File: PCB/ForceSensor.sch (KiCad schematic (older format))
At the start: 8 parts

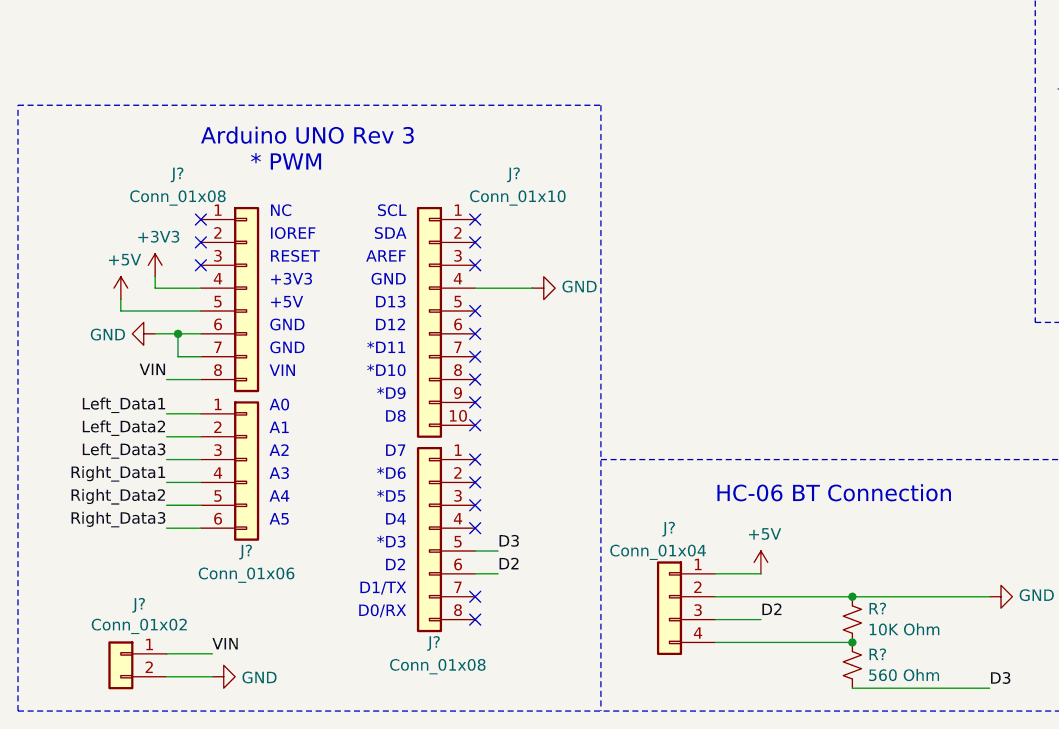
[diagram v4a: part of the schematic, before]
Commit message: Rough layout of pcb
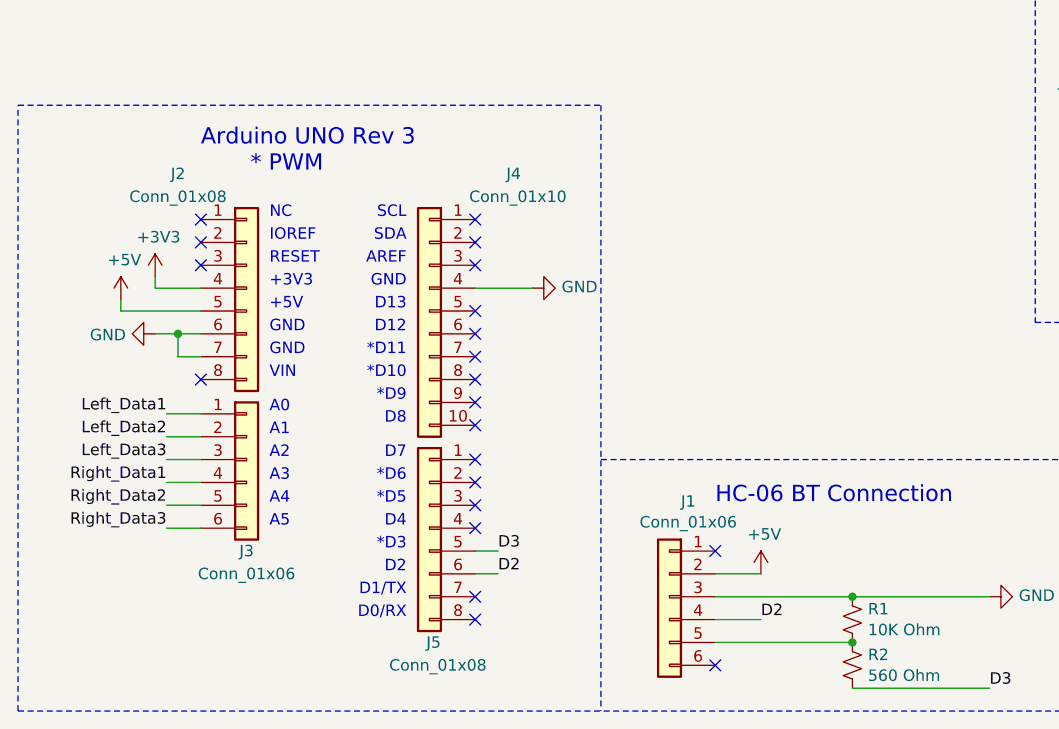
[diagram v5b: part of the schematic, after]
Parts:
- removed J?: Conn_01x04, symbol Connector_Generic:Conn_01x04
- removed J?: Conn_01x02, symbol Connector_Generic:Conn_01x02
- added J1: Conn_01x06, Connector_PinHeader_2.54mm:PinHeader_1x06_P2.54mm_Vertical, symbol Connector_Generic:Conn_01x06
- J2, J5: renamed from J?; footprint (none) -> Connector_PinHeader_2.54mm:PinHeader_1x08_P2.54mm_Vertical
- J3: renamed from J?; footprint (none) -> Connector_PinHeader_2.54mm:PinHeader_1x06_P2.54mm_Vertical
- J4: renamed from J?; footprint (none) -> Connector_PinHeader_2.54mm:PinHeader_1x10_P2.54mm_Vertical
- R1, R2: renamed from R?; footprint (none) -> Resistor_THT:R_Axial_DIN0207_L6.3mm_D2.5mm_P7.62mm_Horizontal
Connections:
- net +5V: now also J1.2 (Pin_2)
- net D2: now also J1.4 (Pin_4)
- net GND: now also J1.3 (Pin_3)
- net at R1.2, R2.1: now also J1.5 (Pin_5)
- net VIN: no longer names the net of J2.8 (Pin_8)
- no-connect marks 18 -> 21
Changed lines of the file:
@@
 $EndDescr
 $Comp
-L Connector_Generic:Conn_01x10 J?
+L Connector_Generic:Conn_01x10 J4
 U 1 1 611AFD66
 P 3850 3100
-F 0 "J?" H 3450 3700 50  0000 L CNN
+F 0 "J4" H 3450 3700 50  0000 L CNN
 F 1 "Conn_01x10" H 3250 3600 50  0000 L CNN
-F 2 "" H 3850 3100 50  0001 C CNN
+F 2 "Connector_PinHeader_2.54mm:PinHeader_1x10_P2.54mm_Vertical" H 3850 3100 50  0001 C CNN
 F 3 "~" H 3850 3100 50  0001 C CNN
 	1    3850 3100
@@
 $EndSheet
 $Comp
-L Connector_Generic:Conn_01x08 J?
+L Connector_Generic:Conn_01x08 J2
 U 1 1 611E4224
 P 3050 3000
-F 0 "J?" H 2750 3500 50  0000 C CNN
+F 0 "J2" H 2750 3500 50  0000 C CNN
 F 1 "Conn_01x08" H 2750 3400 50  0000 C CNN
-F 2 "" H 3050 3000 50  0001 C CNN
+F 2 "Connector_PinHeader_2.54mm:PinHeader_1x08_P2.54mm_Vertical" H 3050 3000 50  0001 C CNN
 F 3 "~" H 3050 3000 50  0001 C CNN
 	1    3050 3000
@@
 $EndComp
 $Comp
-L Connector_Generic:Conn_01x06 J?
+L Connector_Generic:Conn_01x06 J3
 U 1 1 611E4D84
 P 3050 3750
-F 0 "J?" H 3050 3350 50  0000 C CNN
+F 0 "J3" H 3050 3350 50  0000 C CNN
 F 1 "Conn_01x06" H 3050 3250 50  0000 C CNN
-F 2 "" H 3050 3750 50  0001 C CNN
+F 2 "Connector_PinHeader_2.54mm:PinHeader_1x06_P2.54mm_Vertical" H 3050 3750 50  0001 C CNN
 F 3 "~" H 3050 3750 50  0001 C CNN
 	1    3050 3750
@@
 D0/RX
 $Comp
-L Connector_Generic:Conn_01x04 J?
-U 1 1 611DBB38
-P 4900 4350
-AR Path="/611E7D97/611DBB38" Ref="J?"  Part="1"
-AR Path="/611DBB38" Ref="J?"  Part="1"
-F 0 "J?" H 4900 4650 50  0000 C CNN
-F 1 "Conn_01x04" H 4950 4550 50  0000 C CNN
-F 2 "" H 4900 4350 50  0001 C CNN
-F 3 "~" H 4900 4350 50  0001 C CNN
-	1    4900 4350
-	-1   0    0    -1
-$EndComp
-$Comp
 L BPSDisplay:GND #PWR?
 U 1 1 611DBB3F
 P 6300 4350
 AR Path="/611E7D97/611DBB3F" Ref="#PWR?"  Part="1"
-AR Path="/611DBB3F" Ref="#PWR?"  Part="1"
-F 0 "#PWR?" H 6300 4100 50  0001 C CNN
+AR Path="/611DBB3F" Ref="#PWR07"  Part="1"
+F 0 "#PWR07" H 6300 4100 50  0001 C CNN
 F 1 "GND" V 6305 4222 50  0000 R CNN
 F 2 "" H 6300 4350 50  0000 C CNN
@@
 P 5700 4450
 AR Path="/611E7D97/611DBB45" Ref="R?"  Part="1"
-AR Path="/611DBB45" Ref="R?"  Part="1"
-F 0 "R?" H 5768 4496 50  0000 L CNN
+AR Path="/611DBB45" Ref="R1"  Part="1"
+F 0 "R1" H 5768 4496 50  0000 L CNN
 F 1 "10K Ohm" H 5768 4405 50  0000 L CNN
-F 2 "" H 5700 4450 50  0001 C CNN
+F 2 "Resistor_THT:R_Axial_DIN0207_L6.3mm_D2.5mm_P7.62mm_Horizontal" H 5700 4450 50  0001 C CNN
 F 3 "~" H 5700 4450 50  0001 C CNN
 	1    5700 4450
@@
 P 5700 4650
 AR Path="/611E7D97/611DBB4B" Ref="R?"  Part="1"
-AR Path="/611DBB4B" Ref="R?"  Part="1"
-F 0 "R?" H 5768 4696 50  0000 L CNN
+AR Path="/611DBB4B" Ref="R2"  Part="1"
+F 0 "R2" H 5768 4696 50  0000 L CNN
 F 1 "560 Ohm" H 5768 4605 50  0000 L CNN
-F 2 "" H 5700 4650 50  0001 C CNN
+F 2 "Resistor_THT:R_Axial_DIN0207_L6.3mm_D2.5mm_P7.62mm_Horizontal" H 5700 4650 50  0001 C CNN
 F 3 "~" H 5700 4650 50  0001 C CNN
 	1    5700 4650
@@
 	5300 4250 5100 4250
 $Comp
-L power:+3V3 #PWR?
+L power:+3V3 #PWR02
 U 1 1 611DDE98
 P 2650 2950
-F 0 "#PWR?" H 2650 2800 50  0001 C CNN
+F 0 "#PWR02" H 2650 2800 50  0001 C CNN
 F 1 "+3V3" H 2665 3123 50  0000 C CNN
 F 2 "" H 2650 2950 50  0001 C CNN
@@
 $EndComp
 $Comp
-L power:+5V #PWR?
+L power:+5V #PWR01
 U 1 1 611DF2B2
 P 2500 3050
-F 0 "#PWR?" H 2500 2900 50  0001 C CNN
+F 0 "#PWR01" H 2500 2900 50  0001 C CNN
 F 1 "+5V" H 2515 3223 50  0000 C CNN
 F 2 "" H 2500 3050 50  0001 C CNN
@@
 	2500 3100 2850 3100
 $Comp
-L power:GND #PWR?
+L power:GND #PWR03
 U 1 1 611E0B97
 P 2650 3200
-F 0 "#PWR?" H 2650 2950 50  0001 C CNN
+F 0 "#PWR03" H 2650 2950 50  0001 C CNN
 F 1 "GND" V 2655 3072 50  0000 R CNN
 F 2 "" H 2650 3200 50  0001 C CNN
@@
 NoConn ~ 4050 2900
 $Comp
-L power:GND #PWR?
+L power:GND #PWR05
 U 1 1 611E2B05
 P 4300 3000
-F 0 "#PWR?" H 4300 2750 50  0001 C CNN
+F 0 "#PWR05" H 4300 2750 50  0001 C CNN
 F 1 "GND" V 4305 2872 50  0000 R CNN
 F 2 "" H 4300 3000 50  0001 C CNN
@@
 NoConn ~ 4050 4050
 $Comp
-L Connector_Generic:Conn_01x02 J?
-U 1 1 611E52DD
-P 2500 4600
-F 0 "J?" H 2418 4817 50  0000 C CNN
-F 1 "Conn_01x02" H 2418 4726 50  0000 C CNN
-F 2 "" H 2500 4600 50  0001 C CNN
-F 3 "~" H 2500 4600 50  0001 C CNN
-	1    2500 4600
-	-1   0    0    -1
-$EndComp
-$Comp
-L power:GND #PWR?
-U 1 1 611E780E
-P 2900 4700
-F 0 "#PWR?" H 2900 4450 50  0001 C CNN
-F 1 "GND" V 2905 4572 50  0000 R CNN
-F 2 "" H 2900 4700 50  0001 C CNN
-F 3 "" H 2900 4700 50  0001 C CNN
-	1    2900 4700
-	0    -1   1    0
-$EndComp
-Wire Wire Line
-	2700 4600 2900 4600
-Wire Wire Line
-	2900 4700 2700 4700
-Text Label 2900 4600 0    50   ~ 0
-VIN
-Wire Wire Line
-	2850 3400 2700 3400
-Text Label 2700 3400 2    50   ~ 0
-VIN
-$Comp
-L power:+5V #PWR?
+L power:+5V #PWR06
 U 1 1 611ED85A
 P 5300 4250
-F 0 "#PWR?" H 5300 4100 50  0001 C CNN
+F 0 "#PWR06" H 5300 4100 50  0001 C CNN
 F 1 "+5V" H 5315 4423 50  0000 C CNN
 F 2 "" H 5300 4250 50  0001 C CNN
@@
 D2
 $Comp
-L Connector_Generic:Conn_01x08 J?
+L Connector_Generic:Conn_01x08 J5
 U 1 1 611E3554
 P 3850 4050
-F 0 "J?" H 3800 3550 50  0000 L CNN
+F 0 "J5" H 3800 3550 50  0000 L CNN
 F 1 "Conn_01x08" H 3600 3450 50  0000 L CNN
-F 2 "" H 3850 4050 50  0001 C CNN
+F 2 "Connector_PinHeader_2.54mm:PinHeader_1x08_P2.54mm_Vertical" H 3850 4050 50  0001 C CNN
 F 3 "~" H 3850 4050 50  0001 C CNN
 	1    3850 4050
@@
 D3
 $Comp
-L power:+5V #PWR?
+L power:+5V #PWR08
 U 1 1 611F02A4
 P 6650 2300
-F 0 "#PWR?" H 6650 2150 50  0001 C CNN
+F 0 "#PWR08" H 6650 2150 50  0001 C CNN
 F 1 "+5V" H 6665 2473 50  0000 C CNN
 F 2 "" H 6650 2300 50  0001 C CNN
@@
 $EndComp
 $Comp
-L power:+5V #PWR?
+L power:+5V #PWR09
 U 1 1 611F08C5
 P 8550 2300
-F 0 "#PWR?" H 8550 2150 50  0001 C CNN
+F 0 "#PWR09" H 8550 2150 50  0001 C CNN
 F 1 "+5V" H 8565 2473 50  0000 C CNN
 F 2 "" H 8550 2300 50  0001 C CNN
@@
 Wire Notes Line
 	10500 1700 10500 3150
+NoConn ~ 2850 3400
+$Comp
+L Connector_Generic:Conn_01x06 J1
+U 1 1 6125ACCA
+P 4900 4350
+F 0 "J1" H 4818 4767 50  0000 C CNN
+F 1 "Conn_01x06" H 4818 4676 50  0000 C CNN
+F 2 "Connector_PinHeader_2.54mm:PinHeader_1x06_P2.54mm_Vertical" H 4900 4350 50  0001 C CNN
+F 3 "~" H 4900 4350 50  0001 C CNN
+	1    4900 4350
+	-1   0    0    -1
+$EndComp
+NoConn ~ 5100 4150
+NoConn ~ 5100 4650
 $EndSCHEMATC

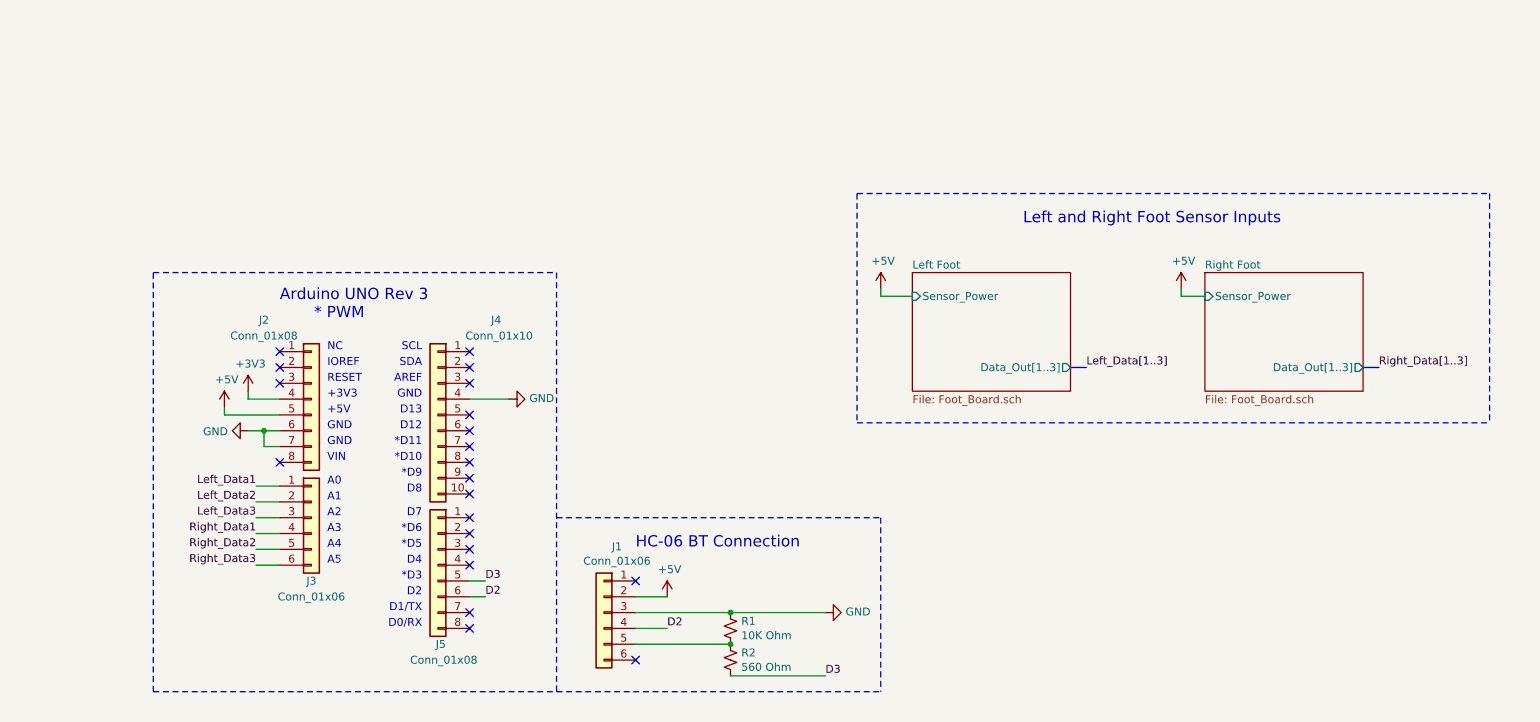
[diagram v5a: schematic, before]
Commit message: Added power LED
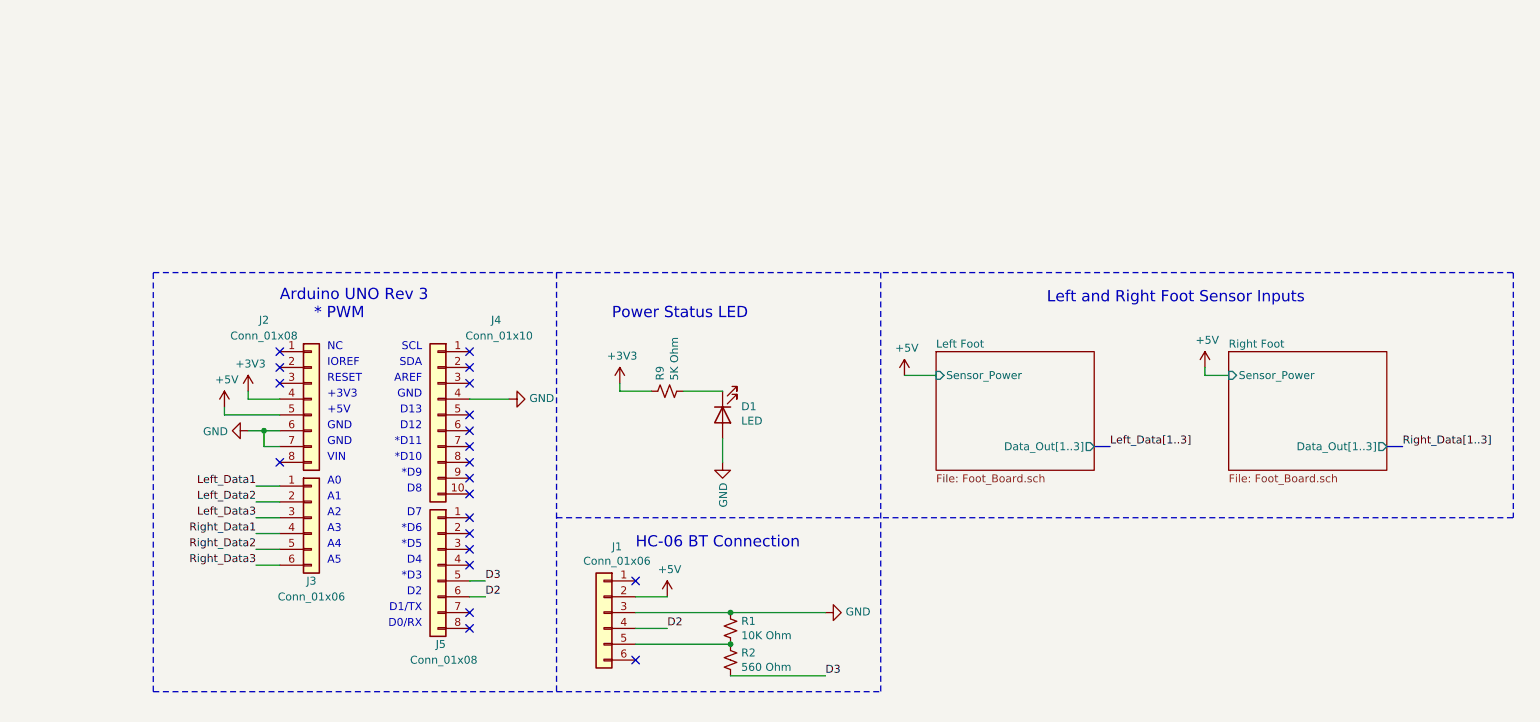
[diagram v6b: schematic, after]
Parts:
- added D1: LED, Diode_THT:D_T-1_P2.54mm_Vertical_AnodeUp, symbol Device:LED
- added R9: 5K Ohm, Resistor_THT:R_Axial_DIN0207_L6.3mm_D2.5mm_P7.62mm_Horizontal, symbol Device:R_Small_US
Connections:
- net +3V3: now also R9.1
- net GND: now also D1.2 (A)
- new net: D1.1 (K), R9.2
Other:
- note added: "Power Status LED"
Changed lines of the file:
@@
 Arduino UNO Rev 3\n       * PWM
 $Sheet
-S 6850 2200 1000 750
+S 7000 2700 1000 750
 U 611C8367
 F0 "Left Foot" 50
 F1 "Foot_Board.sch" 50
-F2 "Sensor_Power" I L 6850 2350 50
-F3 "Data_Out[1..3]" O R 7850 2800 50
+F2 "Sensor_Power" I L 7000 2850 50
+F3 "Data_Out[1..3]" O R 8000 3300 50
 $EndSheet
 $Sheet
-S 8700 2200 1000 750
+S 8850 2700 1000 750
 U 611CB06B
 F0 "Right Foot" 50
 F1 "Foot_Board.sch" 50
-F2 "Sensor_Power" I L 8700 2350 50
-F3 "Data_Out[1..3]" O R 9700 2800 50
+F2 "Sensor_Power" I L 8850 2850 50
+F3 "Data_Out[1..3]" O R 9850 3300 50
 $EndSheet
 $Comp
@@
 L power:+3V3 #PWR02
 U 1 1 611DDE98
-P 2650 2950
-F 0 "#PWR02" H 2650 2800 50  0001 C CNN
-F 1 "+3V3" H 2665 3123 50  0000 C CNN
-F 2 "" H 2650 2950 50  0001 C CNN
-F 3 "" H 2650 2950 50  0001 C CNN
-	1    2650 2950
+P 5000 2900
+F 0 "#PWR02" H 5000 2750 50  0001 C CNN
+F 1 "+3V3" H 5015 3073 50  0000 C CNN
+F 2 "" H 5000 2900 50  0001 C CNN
+F 3 "" H 5000 2900 50  0001 C CNN
+	1    5000 2900
 	1    0    0    -1
 $EndComp
@@
 L power:+5V #PWR08
 U 1 1 611F02A4
-P 6650 2300
-F 0 "#PWR08" H 6650 2150 50  0001 C CNN
-F 1 "+5V" H 6665 2473 50  0000 C CNN
-F 2 "" H 6650 2300 50  0001 C CNN
-F 3 "" H 6650 2300 50  0001 C CNN
-	1    6650 2300
+P 6800 2850
+F 0 "#PWR08" H 6800 2700 50  0001 C CNN
+F 1 "+5V" H 6815 3023 50  0000 C CNN
+F 2 "" H 6800 2850 50  0001 C CNN
+F 3 "" H 6800 2850 50  0001 C CNN
+	1    6800 2850
 	1    0    0    -1
 $EndComp
@@
 L power:+5V #PWR09
 U 1 1 611F08C5
-P 8550 2300
-F 0 "#PWR09" H 8550 2150 50  0001 C CNN
-F 1 "+5V" H 8565 2473 50  0000 C CNN
-F 2 "" H 8550 2300 50  0001 C CNN
-F 3 "" H 8550 2300 50  0001 C CNN
-	1    8550 2300
-	1    0    0    -1
-$EndComp
-Wire Wire Line
-	6650 2300 6650 2350
-Wire Wire Line
-	6650 2350 6850 2350
-Wire Wire Line
-	8550 2300 8550 2350
-Wire Wire Line
-	8550 2350 8700 2350
+P 8700 2800
+F 0 "#PWR09" H 8700 2650 50  0001 C CNN
+F 1 "+5V" H 8715 2973 50  0000 C CNN
+F 2 "" H 8700 2800 50  0001 C CNN
+F 3 "" H 8700 2800 50  0001 C CNN
+	1    8700 2800
+	1    0    0    -1
+$EndComp
+Wire Wire Line
+	6800 2850 7000 2850
+Wire Wire Line
+	8700 2800 8700 2850
+Wire Wire Line
+	8700 2850 8850 2850
 Wire Notes Line
 	2050 4850 2050 2200
-Wire Notes Line
-	2050 2200 4600 2200
 Wire Bus Line
-	7850 2800 7950 2800
+	8000 3300 8100 3300
 Wire Bus Line
-	9700 2800 9800 2800
-Text Label 9800 2800 0    50   ~ 0
+	9850 3300 9950 3300
+Text Label 9950 3300 0    50   ~ 0
 Right_Data[1..3]
-Text Label 7950 2800 0    50   ~ 0
+Text Label 8100 3300 0    50   ~ 0
 Left_Data[1..3]
 Text Label 2700 3550 2    50   ~ 0
@@
 HC-06 BT Connection
 Wire Notes Line
-	4600 3750 6650 3750
-Wire Notes Line
-	6650 3750 6650 4850
-Wire Notes Line
 	4600 2200 4600 4850
 Wire Notes Line
 	2050 4850 6650 4850
-Wire Notes Line
-	6500 1700 10500 1700
-Wire Notes Line
-	6500 3150 10500 3150
-Text Notes 7550 1900 0    71   ~ 0
+Text Notes 7700 2400 0    71   ~ 0
 Left and Right Foot Sensor Inputs
-Wire Notes Line
-	6500 1700 6500 3150
-Wire Notes Line
-	10500 1700 10500 3150
 NoConn ~ 2850 3400
 $Comp
@@
 NoConn ~ 5100 4150
 NoConn ~ 5100 4650
+$Comp
+L Device:LED D1
+U 1 1 612997DC
+P 5650 3100
+F 0 "D1" V 5597 2982 50  0000 R CNN
+F 1 "LED" V 5688 2982 50  0000 R CNN
+F 2 "Diode_THT:D_T-1_P2.54mm_Vertical_AnodeUp" H 5650 3100 50  0001 C CNN
+F 3 "~" H 5650 3100 50  0001 C CNN
+	1    5650 3100
+	0    -1   1    0
+$EndComp
+$Comp
+L Device:R_Small_US R?
+U 1 1 61299FC5
+P 5300 2950
+AR Path="/611E7D97/61299FC5" Ref="R?"  Part="1"
+AR Path="/61299FC5" Ref="R9"  Part="1"
+F 0 "R9" H 5368 2996 50  0000 L CNN
+F 1 "5K Ohm" H 5368 2905 50  0000 L CNN
+F 2 "Resistor_THT:R_Axial_DIN0207_L6.3mm_D2.5mm_P7.62mm_Horizontal" H 5300 2950 50  0001 C CNN
+F 3 "~" H 5300 2950 50  0001 C CNN
+	1    5300 2950
+	0    -1   -1   0
+$EndComp
+$Comp
+L BPSDisplay:GND #PWR?
+U 1 1 6129C000
+P 5650 3400
+AR Path="/611E7D97/6129C000" Ref="#PWR?"  Part="1"
+AR Path="/6129C000" Ref="#PWR016"  Part="1"
+F 0 "#PWR016" H 5650 3150 50  0001 C CNN
+F 1 "GND" V 5655 3272 50  0000 R CNN
+F 2 "" H 5650 3400 50  0000 C CNN
+F 3 "" H 5650 3400 50  0000 C CNN
+	1    5650 3400
+	1    0    0    -1
+$EndComp
+Wire Wire Line
+	5650 2950 5400 2950
+Wire Wire Line
+	5650 3250 5650 3400
+Wire Wire Line
+	5000 2950 5200 2950
+Wire Wire Line
+	5000 2900 5000 2950
+Text Notes 4950 2500 0    71   ~ 0
+Power Status LED
+Wire Notes Line
+	6650 2200 6650 4850
+Wire Notes Line
+	4600 3750 10650 3750
+Wire Notes Line
+	2050 2200 10650 2200
+Wire Notes Line
+	10650 2200 10650 3750
+$Comp
+L power:+3V3 #PWR04
+U 1 1 612A6CAE
+P 2650 2950
+F 0 "#PWR04" H 2650 2800 50  0001 C CNN
+F 1 "+3V3" H 2665 3123 50  0000 C CNN
+F 2 "" H 2650 2950 50  0001 C CNN
+F 3 "" H 2650 2950 50  0001 C CNN
+	1    2650 2950
+	1    0    0    -1
+$EndComp
 $EndSCHEMATC
